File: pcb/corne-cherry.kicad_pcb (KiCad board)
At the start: 2 copper layers, 275.5 x 105.6 mm, 176 parts, among them J1 MJ-4PP-9, J2 OLED, J3 MJ-4PP-9, J4 OLED, J5 Conn_01x01_Male, J6 Conn_01x01_Male, P1 Conn_01x03, P3 Conn_01x03, SW1 SW_PUSH, SW10 SW_PUSH, SW11 SW_PUSH, SW12 SW_PUSH, SW13 SW_PUSH, SW14 SW_PUSH, SW15 SW_PUSH, SW16 SW_PUSH, SW17 SW_PUSH, SW18 SW_PUSH, SW19 SW_PUSH, SW2 SW_PUSH, SW20 SW_PUSH, SW21 SW_PUSH, SW22 SW_PUSH, SW23 SW_PUSH, SW24 SW_PUSH, SW25 SW_PUSH, SW26 SW_PUSH, SW27 SW_PUSH, SW28 SW_PUSH, SW29 SW_PUSH, SW3 SW_PUSH, SW30 SW_PUSH, SW31 SW_PUSH, SW32 SW_PUSH, SW33 SW_PUSH, SW34 SW_PUSH, SW35 SW_PUSH, SW36 SW_PUSH, SW37 SW_PUSH, SW38 SW_PUSH, SW39 SW_PUSH, SW4 SW_PUSH, SW40 SW_PUSH, SW41 SW_PUSH, SW42 SW_PUSH, SW43 Rotary_Encoder_Switch, SW44 Rotary_Encoder_Switch, SW5 SW_PUSH, SW6 SW_PUSH, SW7 SW_PUSH, SW8 SW_PUSH, SW9 SW_PUSH, U1 ProMicro, U2 ProMicro

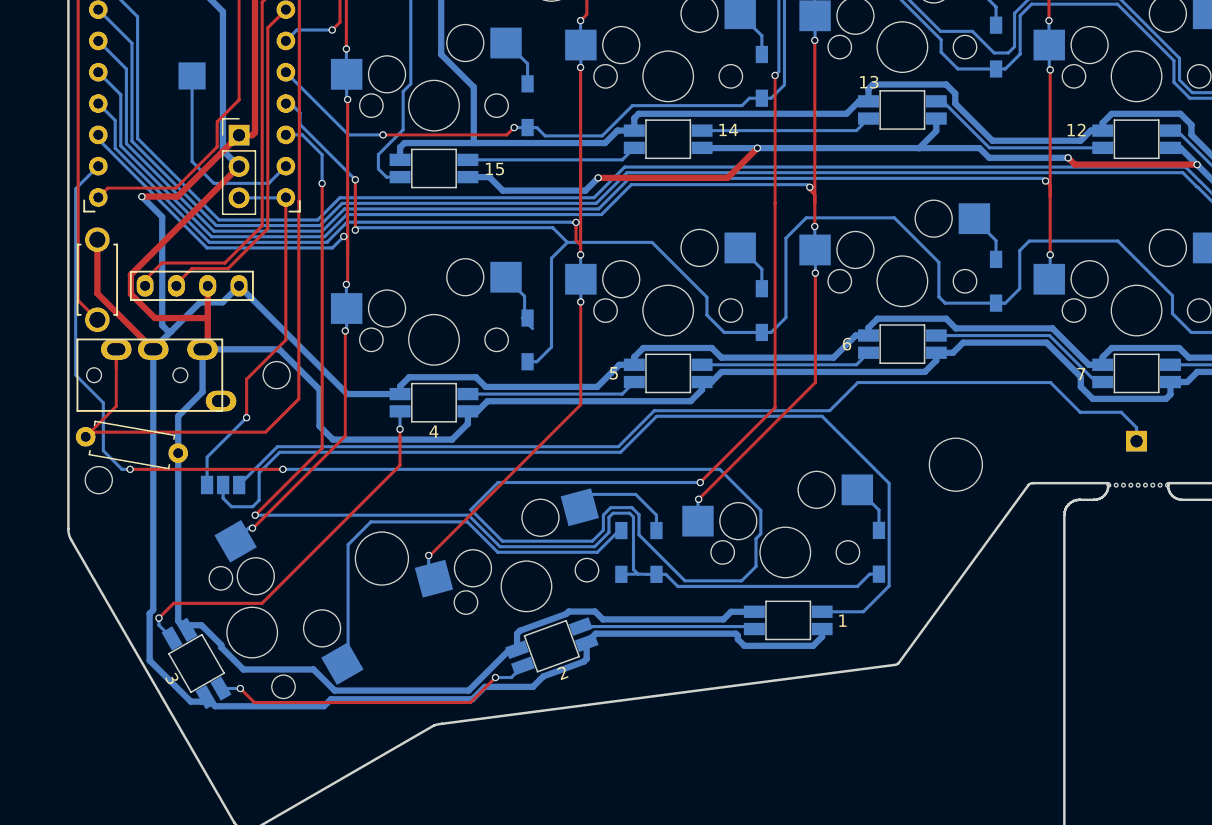
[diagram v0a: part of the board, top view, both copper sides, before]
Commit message: Add trackball support
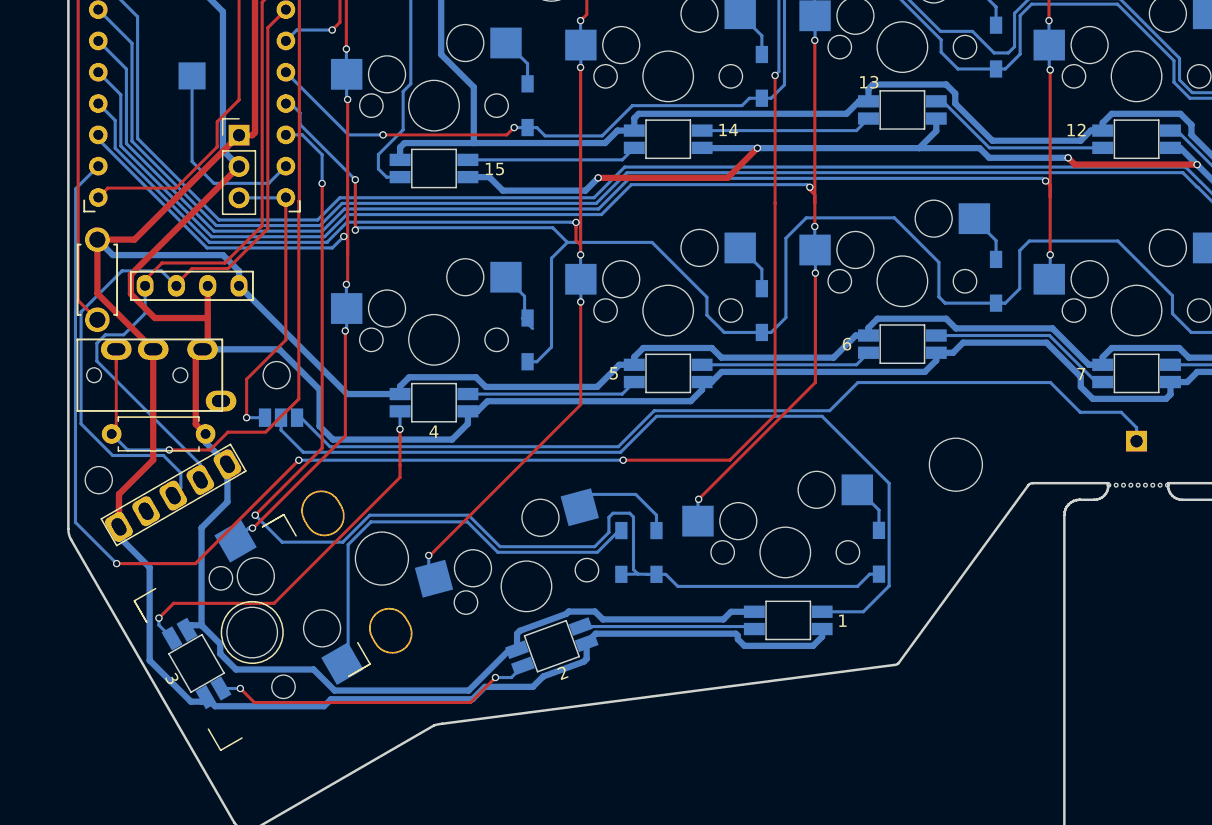
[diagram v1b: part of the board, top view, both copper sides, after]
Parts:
- added J7: Conn_01x05, other_parts:pimoroni_left_side_mount, B.Cu at (166.9, 95.1)
- moved JP2 7.20 mm to (169.2, 77.7)
- moved R2 2.12 mm to (155.5, 79.0), turned to 0 degrees
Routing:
- net ENC_A_R: track 257.1 -> 207.7 mm
- net SCL_r: track 27.9 -> 58.4 mm
- net SDA_r: track 32.7 -> 54.4 mm
- net Net-(JP2-Pad2): track 76.6 -> 69.2 mm
- net LED_r: track 29.8 -> 24.5 mm
- net Net-(J6-Pad1): track 78.9 -> 73.9 mm
- net data_r: track 72.5 -> 70.2 mm, vias 0 -> 1
- net row3_r: track 95.3 -> 97.1 mm
- net VDD: track 536.0 -> 537.0 mm
- net Net-(LED24-Pad4): track 31.2 -> 31.7 mm
- net GNDA: track 564.7 -> 564.5 mm, vias 6 -> 5

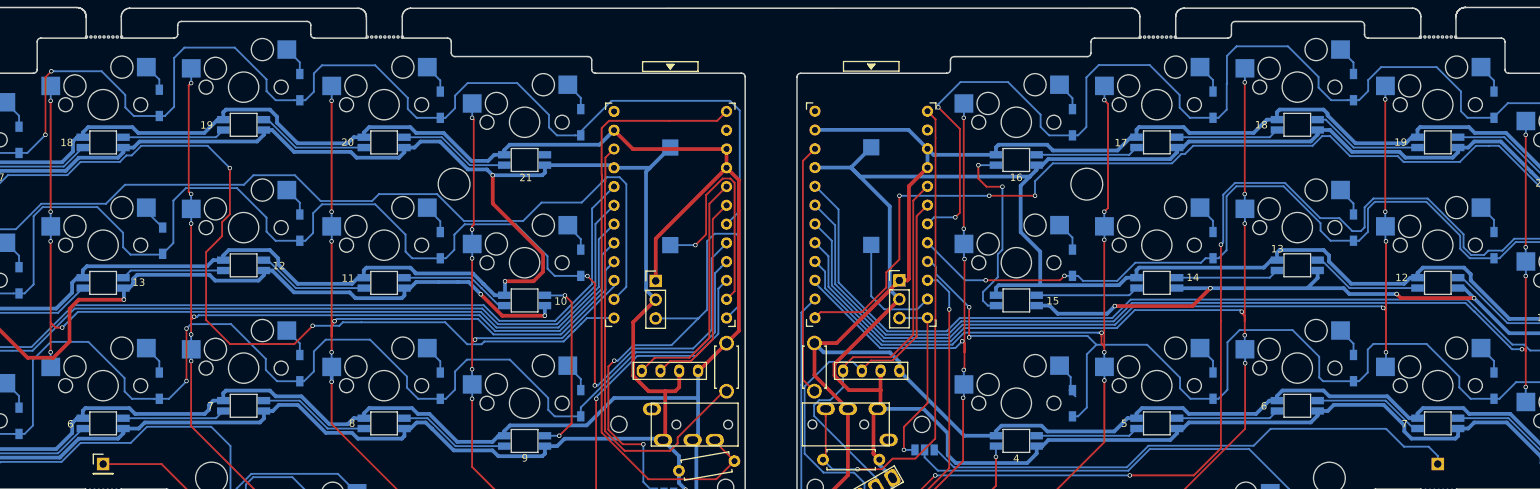
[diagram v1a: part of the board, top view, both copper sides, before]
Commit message: Update markers and silkscreen
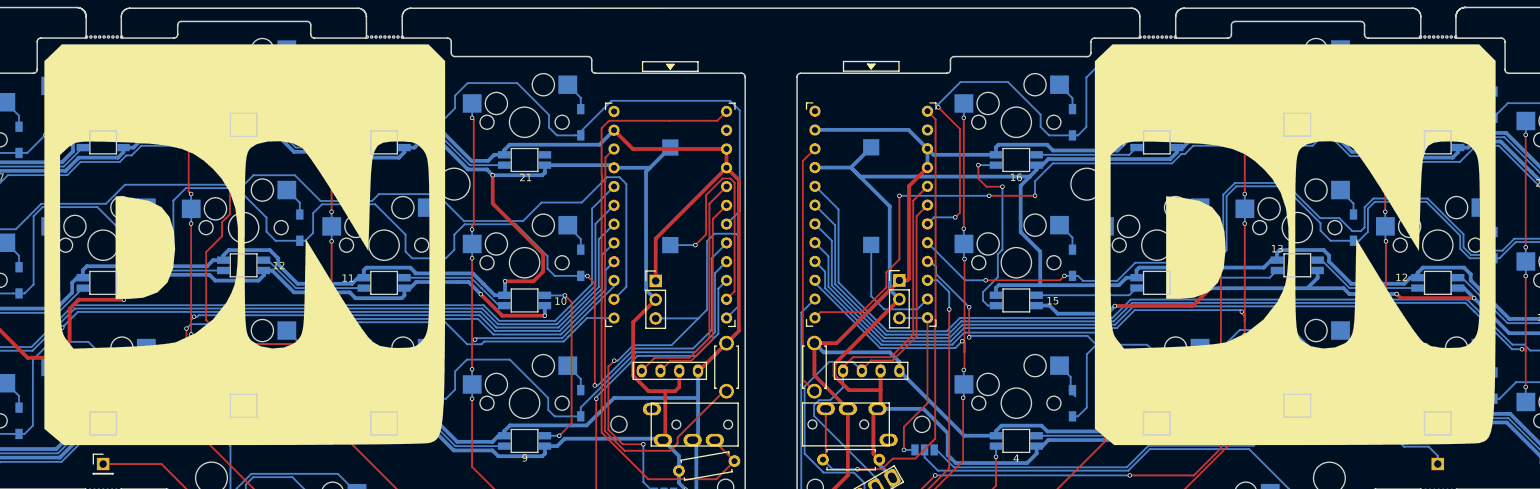
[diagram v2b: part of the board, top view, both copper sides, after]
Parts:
- added G***: LOGO, silks:dn_f, F.Cu at (77.3, 50.0)
- added G***: LOGO, silks:dn_f, F.Cu at (219.3, 50.0)
- J1, J3: value MJ-4PP-9 -> TRRS
- J7: value Conn_01x05 -> Trackball
- P1, P3: value Conn_01x03 -> RGB Header

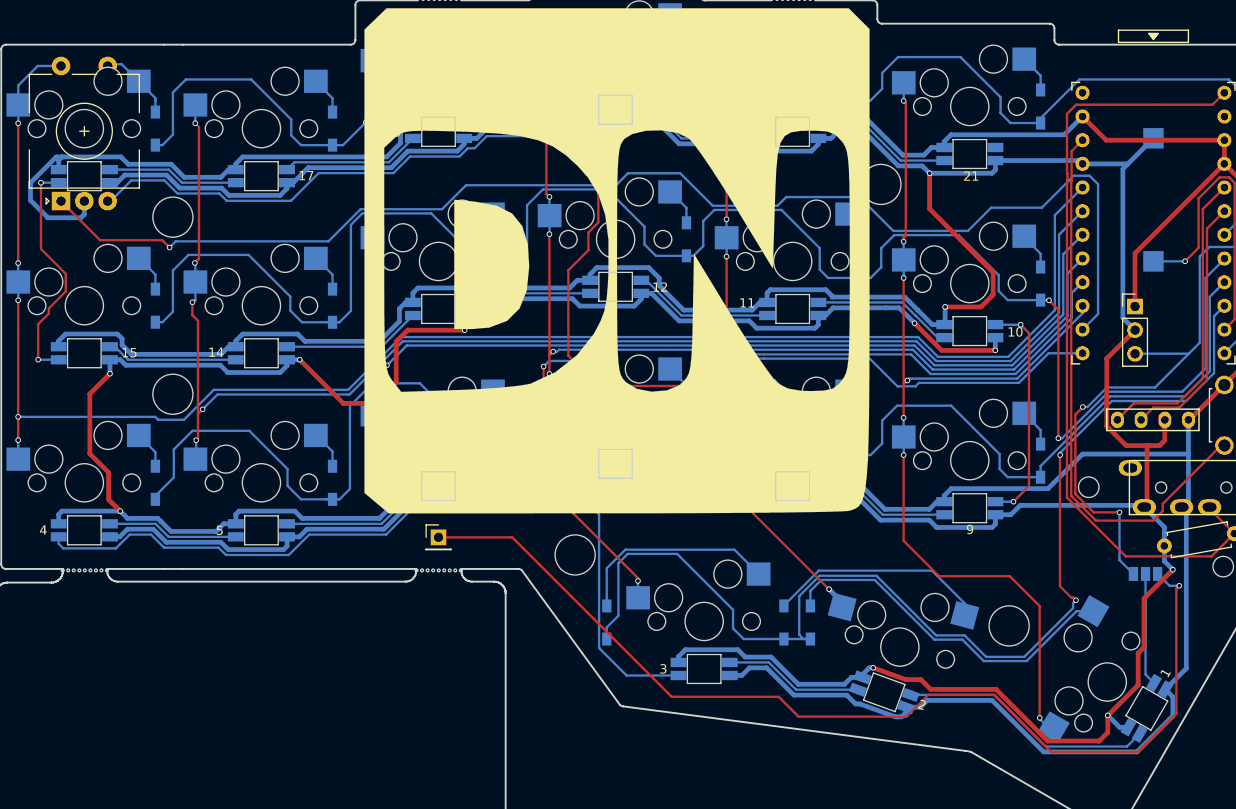
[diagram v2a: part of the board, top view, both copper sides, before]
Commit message: some underglow stuff on left half
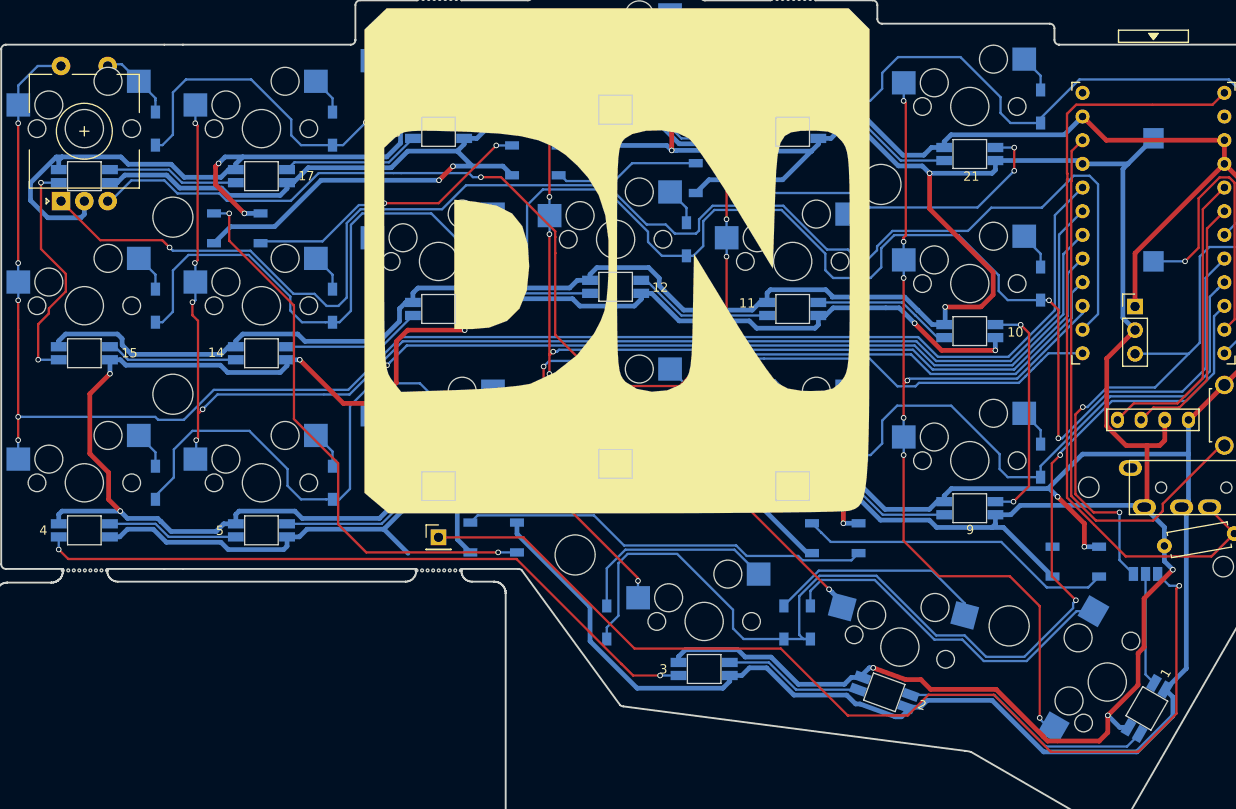
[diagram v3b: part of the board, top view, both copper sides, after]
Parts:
- added D43: WS2812B, Keebio-Parts:WS2812B, B.Cu at (88.2, 41.1)
- added D44: WS2812B, Keebio-Parts:WS2812B, B.Cu at (126.5, 82.2)
- added D45: WS2812B, Keebio-Parts:WS2812B, B.Cu at (68.5, 39.2)
- added D46: WS2812B, Keebio-Parts:WS2812B, B.Cu at (100.7, 79.7)
- added D47: WS2812B, Keebio-Parts:WS2812B, B.Cu at (36.5, 46.5)
- added D48: WS2812B, Keebio-Parts:WS2812B, B.Cu at (64.0, 79.6)
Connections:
- LED18 pad 2: Net-(LED18-Pad2) -> uglow
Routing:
- net GND: track 569.8 -> 663.6 mm, vias 6 -> 14
- net VCC: track 512.9 -> 591.0 mm, vias 5 -> 7
- net Net-(D47-Pad2): track 0.00 -> 60.3 mm, vias 0 -> 2
- net Net-(D46-Pad4): track 0.00 -> 44.3 mm
- net uglow: track 0.00 -> 36.0 mm, vias 0 -> 2
- net Net-(D44-Pad4): track 0.00 -> 34.1 mm
- net Net-(D45-Pad2): track 0.00 -> 31.3 mm, vias 0 -> 2
- net Net-(D43-Pad2): track 0.00 -> 15.8 mm
- net Net-(LED13-Pad2): track 88.5 -> 73.5 mm, vias 0 -> 2
- net ENC_A: track 140.1 -> 154.2 mm
- net ENC_B: track 141.2 -> 127.8 mm
- net row1: track 192.4 -> 191.6 mm
- net row3: track 121.7 -> 122.3 mm

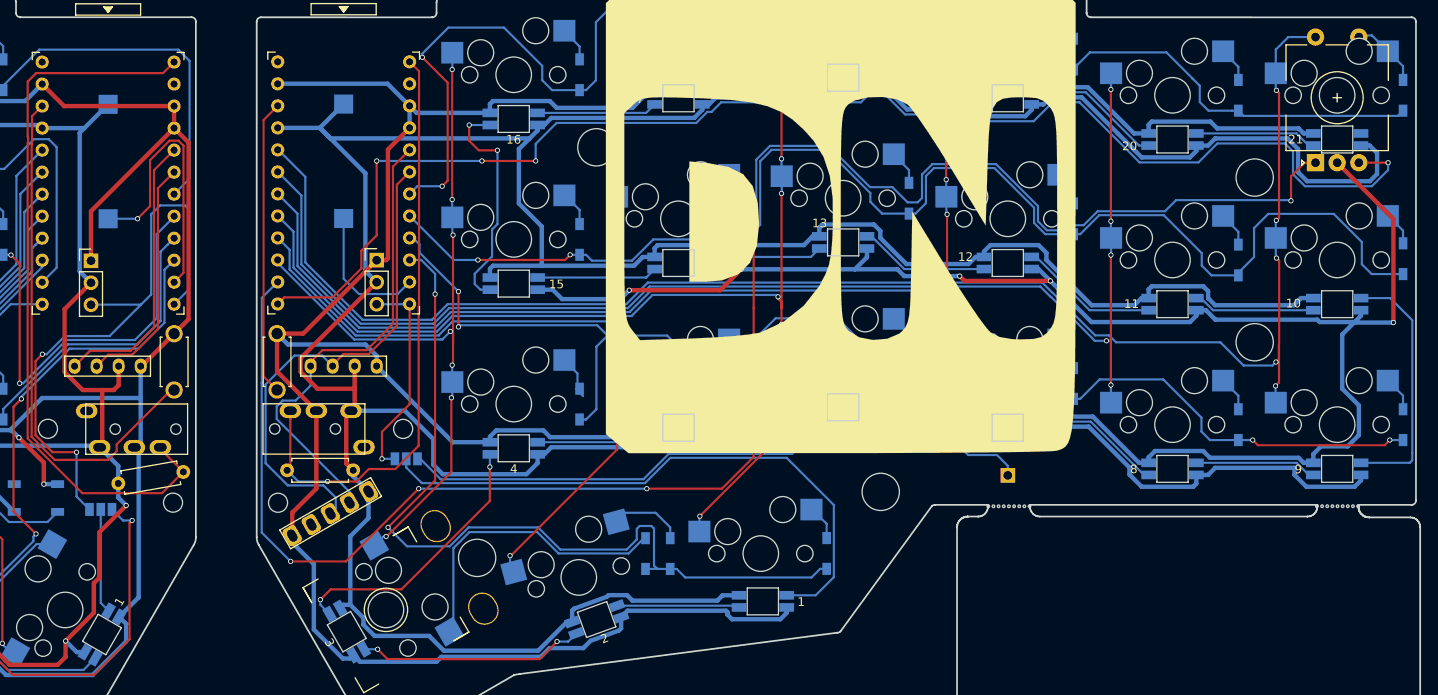
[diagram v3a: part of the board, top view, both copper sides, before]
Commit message: Finish underglow and add SMD resistor foorprints
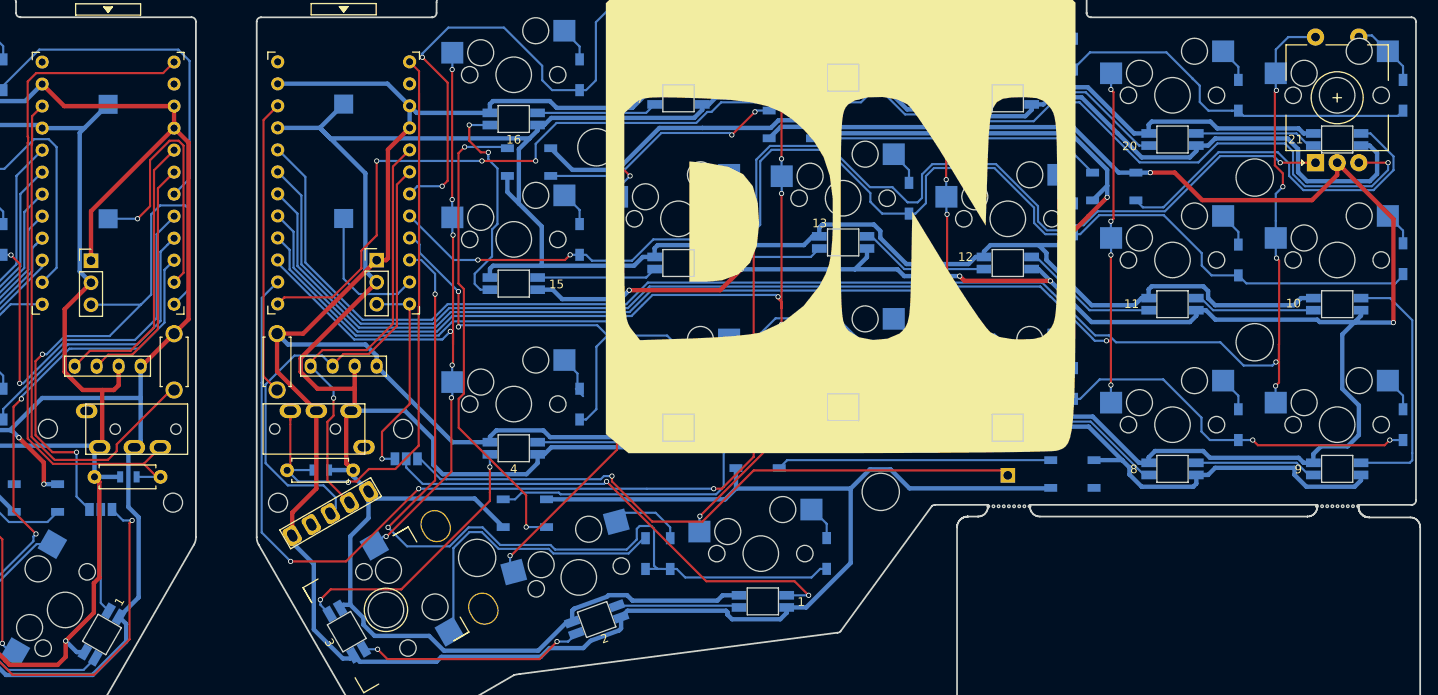
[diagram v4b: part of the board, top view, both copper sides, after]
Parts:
- added D49: WS2812B, Keebio-Parts:WS2812B, B.Cu at (250.9, 46.3)
- added D50: WS2812B, Keebio-Parts:WS2812B, B.Cu at (246.1, 79.5)
- added D51: WS2812B, Keebio-Parts:WS2812B, B.Cu at (213.6, 39.1)
- added D52: WS2812B, Keebio-Parts:WS2812B, B.Cu at (209.7, 77.2)
- added D53: WS2812B, Keebio-Parts:WS2812B, B.Cu at (183.4, 43.5)
- added D54: WS2812B, Keebio-Parts:WS2812B, B.Cu at (182.9, 84.0)
- added R5: 4.7k, Keebio-Parts:R_0805, B.Cu at (137.2, 79.8)
- added R6: 4.7k, Keebio-Parts:R_0805, B.Cu at (159.4, 79.0)
- moved R1 2.69 mm to (140.9, 79.8), turned to 180 degrees
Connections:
- LED40 pad 2: Net-(LED40-Pad2) -> uglow_r
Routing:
- net GNDA: track 564.5 -> 747.0 mm, vias 5 -> 6
- net VDD: track 537.0 -> 624.5 mm, vias 0 -> 2
- net Net-(D53-Pad2): track 0.00 -> 55.2 mm, vias 0 -> 2
- net uglow_r: track 0.00 -> 42.7 mm
- net Net-(D49-Pad2): track 0.00 -> 34.0 mm
- net Net-(D52-Pad4): track 0.00 -> 32.1 mm
- net Net-(D50-Pad4): track 0.00 -> 31.7 mm
- net Net-(D51-Pad2): track 0.00 -> 28.5 mm, vias 0 -> 2
- net Net-(JP2-Pad2): track 69.2 -> 56.3 mm, vias 0 -> 2
- net row1_r: track 153.2 -> 144.9 mm
- net SDA_r: track 54.4 -> 50.9 mm, vias 0 -> 1
- net data_r: track 70.2 -> 73.3 mm
- net data: track 84.6 -> 81.8 mm
- net GND: track 663.6 -> 664.9 mm
- net col4_r: track 115.5 -> 116.6 mm
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
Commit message: Fix RGB positions
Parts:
- moved D53 8.77 mm to (174.6, 43.0), turned to 180 degrees
- moved D47 8.20 mm to (44.7, 45.5)
- moved D43 7.80 mm to (96.0, 40.5)
- moved D54 4.06 mm to (178.8, 84.0), turned to 180 degrees
- moved D51 3.24 mm to (210.3, 39.2), turned to 180 degrees
- moved D49 1.73 mm to (249.9, 44.9), turned to 180 degrees
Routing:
- net GNDA: track 747.0 -> 716.6 mm, vias 6 -> 7
- net VCC: track 591.9 -> 567.7 mm
- net Net-(D49-Pad2): track 34.0 -> 54.7 mm
- net Net-(D51-Pad2): track 28.5 -> 44.9 mm
- net Net-(D53-Pad2): track 55.2 -> 42.8 mm
- net Net-(D43-Pad2): track 15.8 -> 24.6 mm, vias 0 -> 2
- net GND: track 664.9 -> 673.7 mm, vias 14 -> 16
- net uglow_r: track 42.7 -> 51.1 mm
- net Net-(D45-Pad2): track 31.3 -> 23.2 mm
- net uglow: track 36.0 -> 28.4 mm
- net ENC_B_R: track 160.4 -> 155.7 mm
- net Net-(D42-Pad2): track 34.5 -> 30.7 mm
- net VDD: track 624.5 -> 620.7 mm
- net row3_r: track 97.1 -> 95.3 mm
- net ENC_B: track 127.8 -> 129.5 mm, vias 2 -> 4
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
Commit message: Update silkscreen
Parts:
- moved G*** 3.20 mm to (220.0, 53.1)
- moved G*** 2.98 mm to (77.4, 52.9)

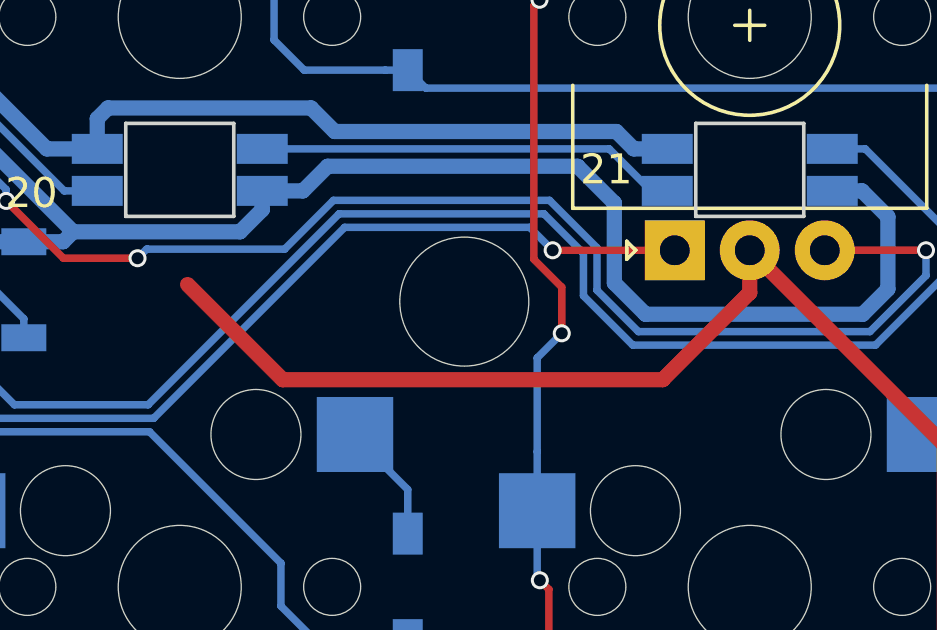
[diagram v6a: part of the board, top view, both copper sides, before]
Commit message: Update firmware and clean up pcb
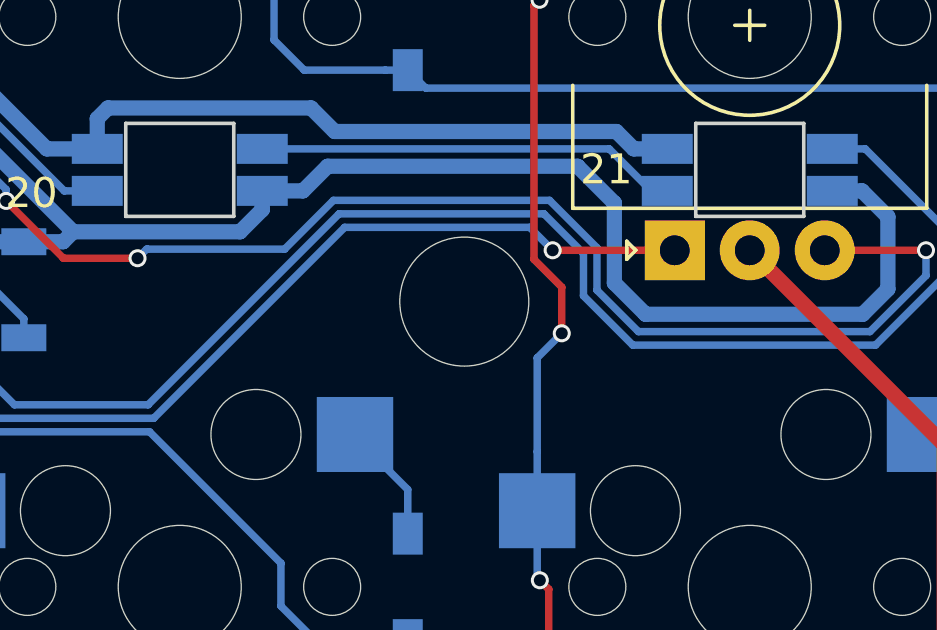
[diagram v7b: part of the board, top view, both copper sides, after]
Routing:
- net GNDA: track 716.6 -> 694.0 mm
